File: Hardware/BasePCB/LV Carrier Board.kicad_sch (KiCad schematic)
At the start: 36 parts, among them J10 Conn_01x02, J11 Conn_01x02, J12 Conn_01x02, J2 Conn_01x04, J3 Conn_01x02, J4 CarCANConnector, J5 Conn_01x02, J8 Conn_01x02, J9 Conn_01x02

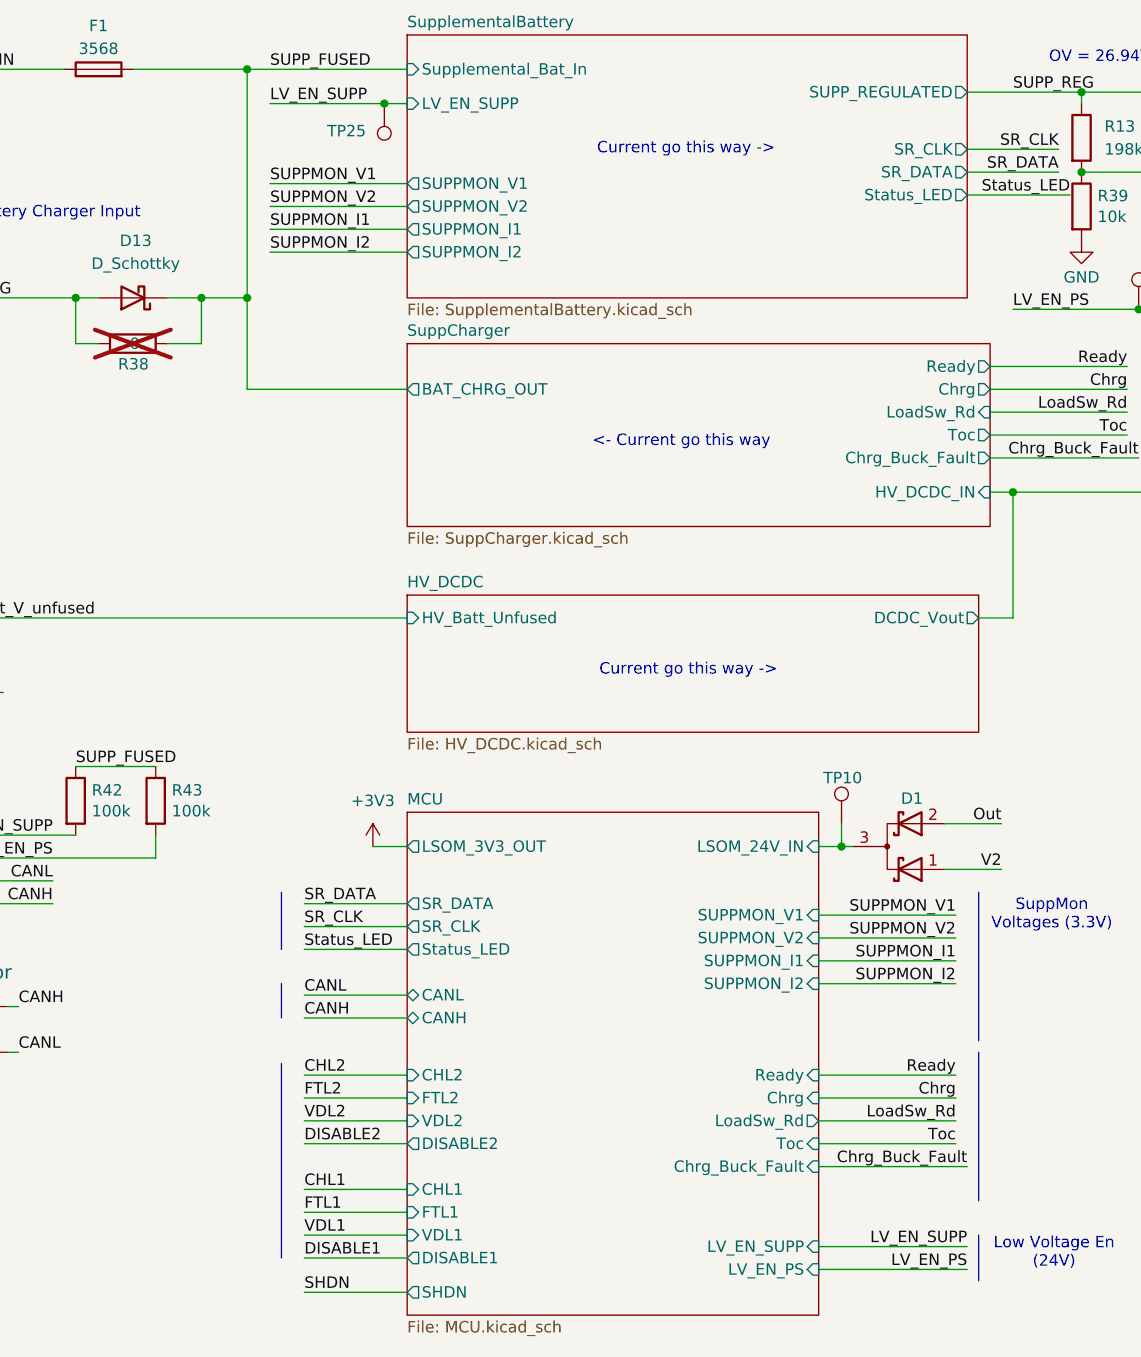
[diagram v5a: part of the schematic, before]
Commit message: add LPF to ADC inputs
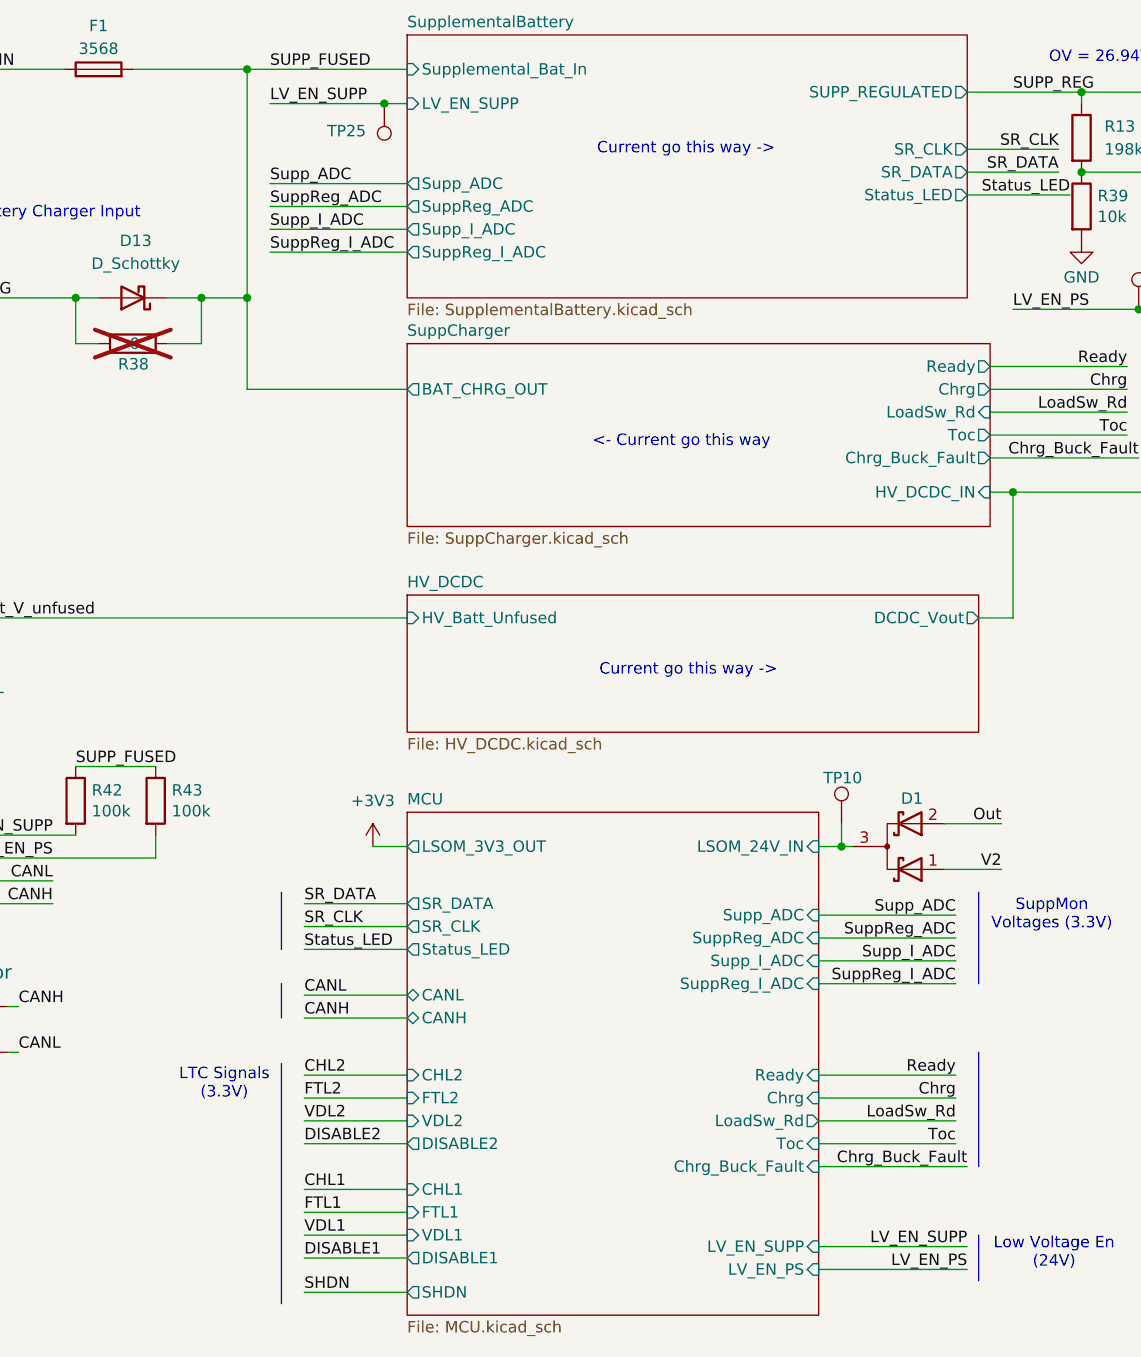
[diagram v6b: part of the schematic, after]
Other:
- sheet MCU ports: added SuppReg_ADC, SuppReg_I_ADC, Supp_ADC, Supp_I_ADC; removed SUPPMON_I1, SUPPMON_I2, SUPPMON_V1, SUPPMON_V2
- sheet SupplementalBattery ports: added SuppReg_ADC, SuppReg_I_ADC, Supp_ADC, Supp_I_ADC; removed SUPPMON_I1, SUPPMON_I2, SUPPMON_V1, SUPPMON_V2
- note added: "LTC Signals (3.3V)"
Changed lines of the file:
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@@
 		)
 	)
+	(text "LTC Signals\n(3.3V)"
+		(exclude_from_sim no)
+		(at 58.42 140.716 0)
+		(effects
+			(font
+				(size 1.27 1.27)
+			)
+		)
+	)
 	(text "Supplemental Battery Input"
 		(exclude_from_sim no)
@@
 	(bus
 		(pts
-			(xy 64.77 138.43) (xy 64.77 160.02)
+			(xy 64.77 138.43) (xy 64.77 165.1)
 		)
 		(stroke
@@
 	(bus
 		(pts
-			(xy 142.24 119.38) (xy 142.24 135.89)
+			(xy 142.24 119.38) (xy 142.24 129.54)
 		)
 		(stroke
@@
 	(bus
 		(pts
-			(xy 142.24 137.16) (xy 142.24 153.67)
+			(xy 142.24 137.16) (xy 142.24 149.86)
 		)
 		(stroke
@@
 		)
 	)
-	(label "SUPPMON_V1"
+	(label "Supp_ADC"
 		(at 63.5 40.64 0)
 		(effects
@@
 		)
 	)
-	(label "SUPPMON_I1"
+	(label "Supp_I_ADC"
 		(at 63.5 45.72 0)
 		(effects
@@
 		)
 	)
-	(label "SUPPMON_I2"
+	(label "SuppReg_I_ADC"
 		(at 139.7 129.54 180)
 		(effects
@@
 		)
 	)
-	(label "SUPPMON_V2"
+	(label "SuppReg_ADC"
 		(at 63.5 43.18 0)
 		(effects
@@
 		)
 	)
-	(label "SUPPMON_I2"
+	(label "SuppReg_I_ADC"
 		(at 63.5 48.26 0)
 		(effects
@@
 		)
 	)
-	(label "SUPPMON_I1"
+	(label "Supp_I_ADC"
 		(at 139.7 127 180)
 		(effects
@@
 		)
 	)
-	(label "SUPPMON_V1"
+	(label "Supp_ADC"
 		(at 139.7 121.92 180)
 		(effects
@@
 		)
 	)
-	(label "SUPPMON_V2"
+	(label "SuppReg_ADC"
 		(at 139.7 124.46 180)
 		(effects
@@
 			)
 		)
-		(pin "SUPPMON_I1" input
+		(pin "Supp_I_ADC" input
 			(at 124.46 127 0)
 			(effects
@@
 			)
 		)
-		(pin "SUPPMON_V1" input
+		(pin "Supp_ADC" input
 			(at 124.46 121.92 0)
 			(effects
@@
 			)
 		)
-		(pin "SUPPMON_V2" input
+		(pin "SuppReg_ADC" input
 			(at 124.46 124.46 0)
 			(effects
@@
 			)
 		)
-		(pin "SUPPMON_I2" input
+		(pin "SuppReg_I_ADC" input
 			(at 124.46 129.54 0)
 			(effects
@@
 			)
 		)
-		(pin "SUPPMON_I2" output
+		(pin "SuppReg_I_ADC" output
 			(at 78.74 48.26 180)
 			(effects
@@
 			)
 		)
-		(pin "SUPPMON_I1" output
+		(pin "Supp_I_ADC" output
 			(at 78.74 45.72 180)
 			(effects
@@
 			)
 		)
-		(pin "SUPPMON_V1" output
+		(pin "Supp_ADC" output
 			(at 78.74 40.64 180)
 			(effects
@@
 			)
 		)
-		(pin "SUPPMON_V2" output
+		(pin "SuppReg_ADC" output
 			(at 78.74 43.18 180)
 			(effects

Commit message: schem done?
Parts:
- renumbered D5 to D2
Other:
- sheet MCU ports: added SuppCharger_En, SuppCharger_Stat1, SuppCharger_Stat2, SuppCharger_~{INT}, {I2C}; removed Chrg, Chrg_Buck_Fault, LoadSw_Rd, Ready, Toc
- sheet SuppCharger ports: added Logic_Rail, SuppCharger_En, SuppCharger_INT, SuppCharger_Stat1, SuppCharger_Stat2, {I2C}; removed Chrg, Chrg_Buck_Fault, LoadSw_Rd, Ready, Toc

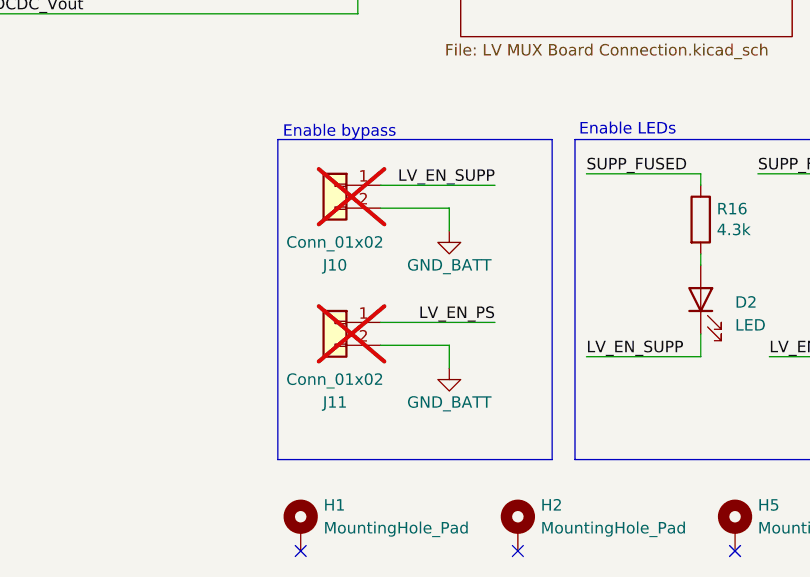
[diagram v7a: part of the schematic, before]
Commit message: supp charger routing done
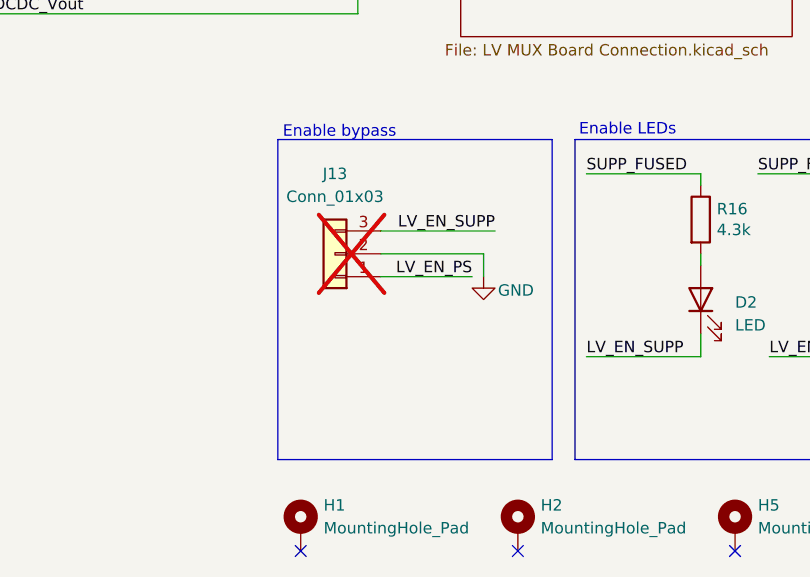
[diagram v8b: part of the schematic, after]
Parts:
- removed J10, J11: Conn_01x02, Connector_PinHeader_2.54mm:PinHeader_1x02_P2.54mm_Vertical, symbol Connector_Generic:Conn_01x02
- added J13: Conn_01x03, Connector_PinHeader_2.54mm:PinHeader_1x03_P2.54mm_Vertical, symbol Connector_Generic:Conn_01x03
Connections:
- net GND: now also J13.2 (Pin_2)
- net LV_EN_PS: now also J13.1 (Pin_1)
- net LV_EN_SUPP: now also J13.3 (Pin_3)
